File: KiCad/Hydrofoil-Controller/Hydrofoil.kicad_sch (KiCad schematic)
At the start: 12 parts, among them J1 Conn_01x03_Pin, J2 Conn_01x03_Pin, U2 LD1117S33CTR, U3 TPS22917DBV

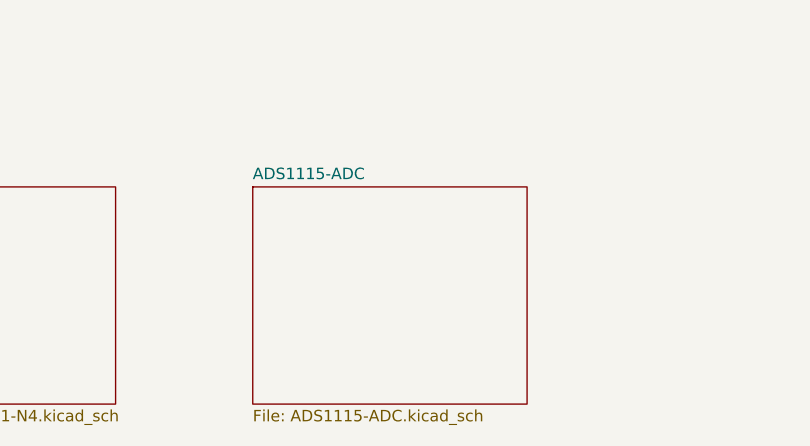
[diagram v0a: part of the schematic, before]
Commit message: Remove ADC from PCB
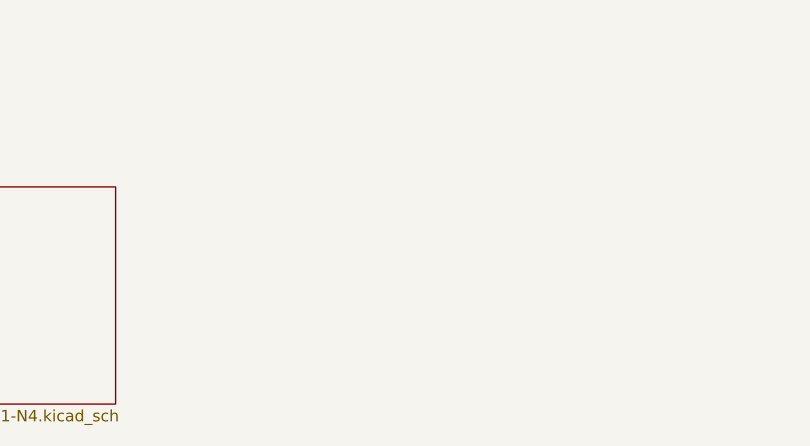
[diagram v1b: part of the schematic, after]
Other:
- removed sheet ADS1115-ADC
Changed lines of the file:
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@@
     (rev "v1.1")
     (company "Tamás Nagy")
+    (comment 1 "ADC removed, capacitance measurement added")
   )

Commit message: Add capacitance measurement to the PCB
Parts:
- J1, J2: MPN (none) -> No Part Required
